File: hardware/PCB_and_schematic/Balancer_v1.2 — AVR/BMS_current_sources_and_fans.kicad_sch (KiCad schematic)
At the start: 87 parts, among them J11 HEATSING_TEMP1, J14 LOAD_RESISTOR, J15 LOAD_RESISTOR, J3 Conn_01x03, J4 HEATSING_TEMP1, J5 FAN1, J6 FAN2, J7 BATT_12V, Q10 BC807, Q11 BC817, Q12 BC817, Q13 BD238, Q14 BC807, Q15 BC817, Q16 BD238, Q18 IRF540N, Q25 IRF540N, Q9 BC817, U1 LM324, U2 74AHCT125, U3 LM358

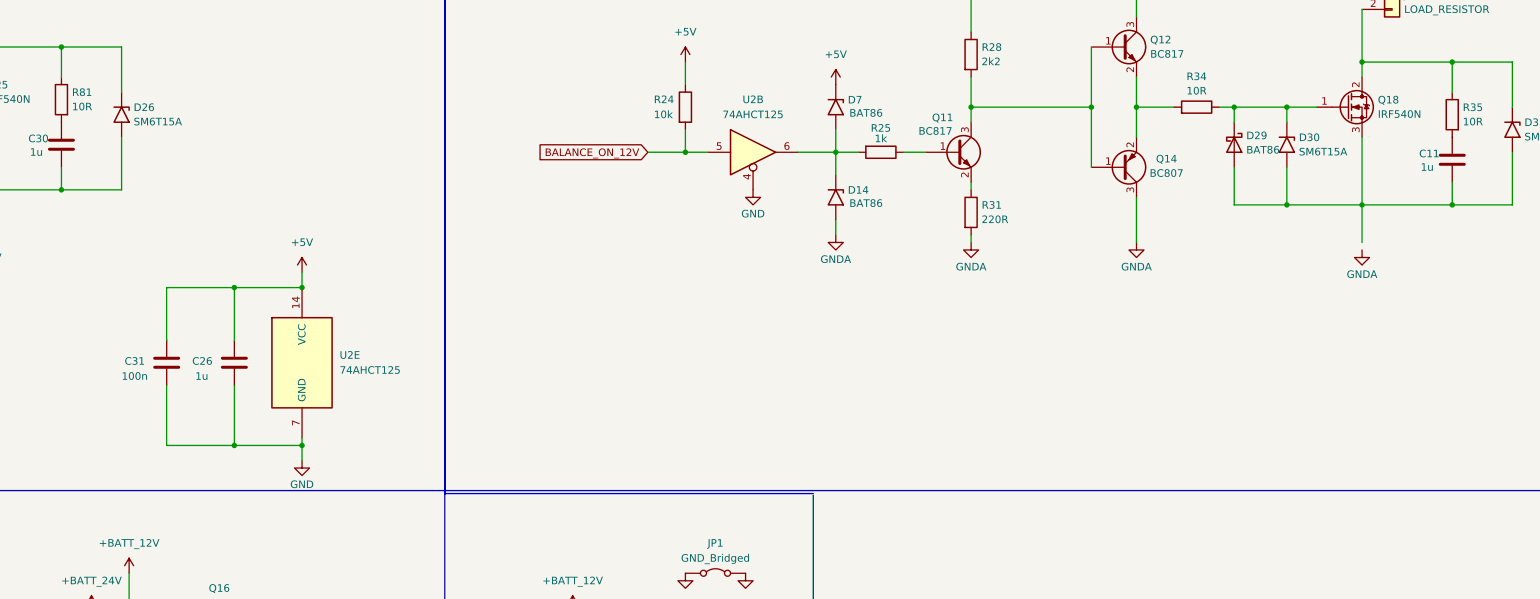
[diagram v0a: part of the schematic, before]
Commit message: Balancer PCB routing
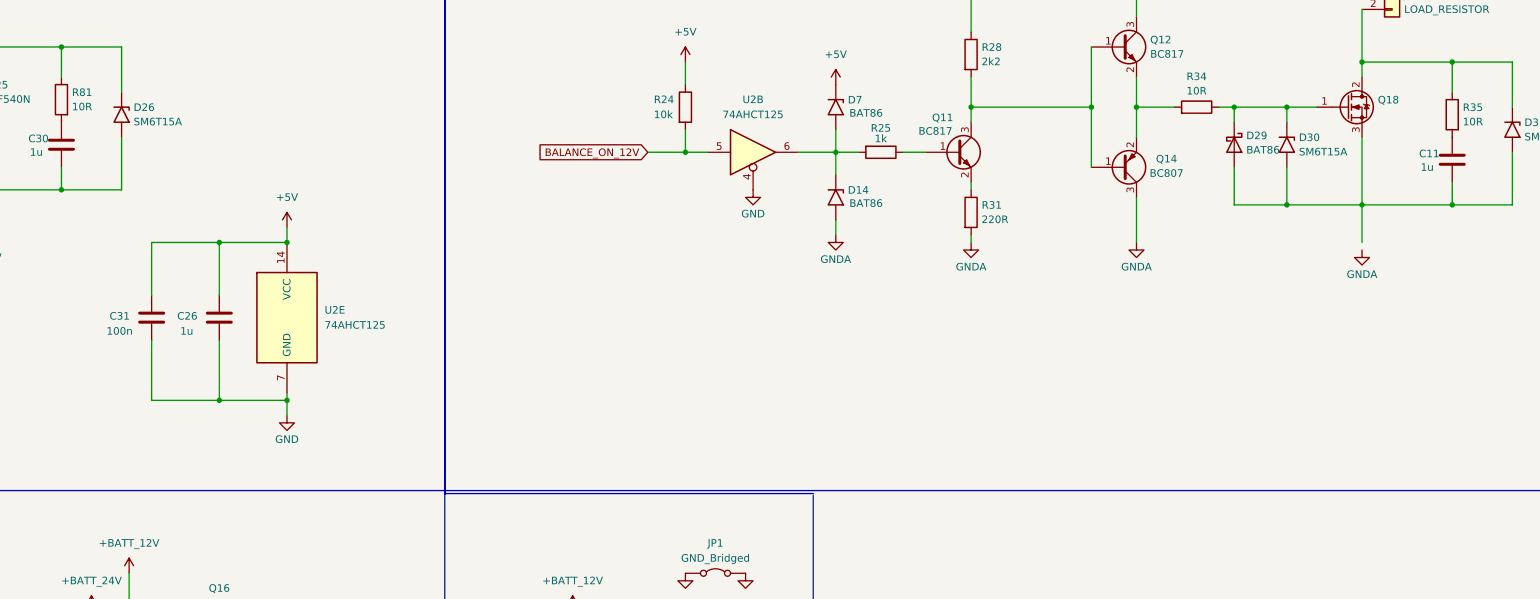
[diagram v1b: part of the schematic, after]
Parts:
- C11, C30: footprint Capacitor_SMD:C_0805_2012Metric_Pad1.18x1.45mm_HandSolder -> Capacitor_THT:C_Disc_D5.0mm_W2.5mm_P2.50mm
- D29: footprint Diode_THT:D_DO-35_SOD27_P7.62mm_Horizontal -> Diode_SMD:D_MiniMELF
- Q13, Q16: footprint My-Footprints:TO-220-3_Vertical-little-bigger pads -> Package_TO_SOT_SMD:SOT-89-3
- R35, R81: footprint Resistor_SMD:R_0805_2012Metric_Pad1.20x1.40mm_HandSolder -> Resistor_THT:R_Axial_DIN0204_L3.6mm_D1.6mm_P7.62mm_Horizontal
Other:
- moved on the sheet: C26, C31, U2E

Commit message: update balancer pcb - add gnd vdrop opamp
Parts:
- removed C7: 100n, Capacitor_SMD:C_0805_2012Metric_Pad1.18x1.45mm_HandSolder, symbol Device:C
- added C37, C39, C40: 100n, Capacitor_SMD:C_0805_2012Metric_Pad1.18x1.45mm_HandSolder, symbol Device:C
- added R60, R61, R62, R63, R66, R67: 10k/1%, Resistor_SMD:R_0805_2012Metric_Pad1.20x1.40mm_HandSolder, symbol Device:R
- added R71: 100R, Resistor_SMD:R_0805_2012Metric_Pad1.20x1.40mm_HandSolder, symbol Device:R
- added U14: LMV358, symbol Amplifier_Operational:LMV358
- U3: footprint Package_SO:SO-8_3.9x4.9mm_P1.27mm -> (none)
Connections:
- net +5V: now also C39.1, U14.8 (V+)
- net +BATT_12V: no longer C5.1, C6.1, Q12.3 (C), R28.1
- net +BATT_24V: no longer C28.1, C29.1, Q9.3 (C), R69.1, U3.8 (V+)
- net GND: now also C37.2, C39.2, C40.2, R62.2, R67.2, U14.4 (V-)
- net GNDA: now also C11.2, D29.2 (A), D30.2 (A2), D31.2 (A2), Q18.3 (S)
- net at C9.1, R30.2, R33.2: now also U3.3 (+); no longer U3.5 (+)
- net at C12.1, R50.2: now also U3.7; no longer U3.1
- net at C13.1, R38.2: now also U3.1; no longer U3.7
- net at C13.2, R40.1: now also U3.2 (-); no longer U3.6 (-)
- net at C12.2, R39.1: now also U3.6 (-); no longer U3.2 (-)
- net at C8.1, R29.2, R32.2: now also U3.5 (+); no longer U3.3 (+)
- new net: R60.2, U14.1, U14.2 (-)
- new net: C37.1, R66.2, R67.1, U14.3 (+)
- new net: R63.1, R71.2, U14.7
- new net: R60.1, R61.1, U14.5 (+)
- new net: R62.1, R63.2, U14.6 (-)
- new net +12V_LOCAL: C5.1, C6.1, Q12.3 (C), R28.1
- new net +24V_LOCAL: C28.1, C29.1, C40.1, Q9.3 (C), R69.1, U3.8 (V+)
- new net GND_VOLTAGE_DROP_ADC: R71.1
- new net GND_VOLTAGE_DROP_INPUT: R61.2
- new net VREF: R66.1
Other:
- note added: "1,25V"
- moved on the sheet: C10, C27

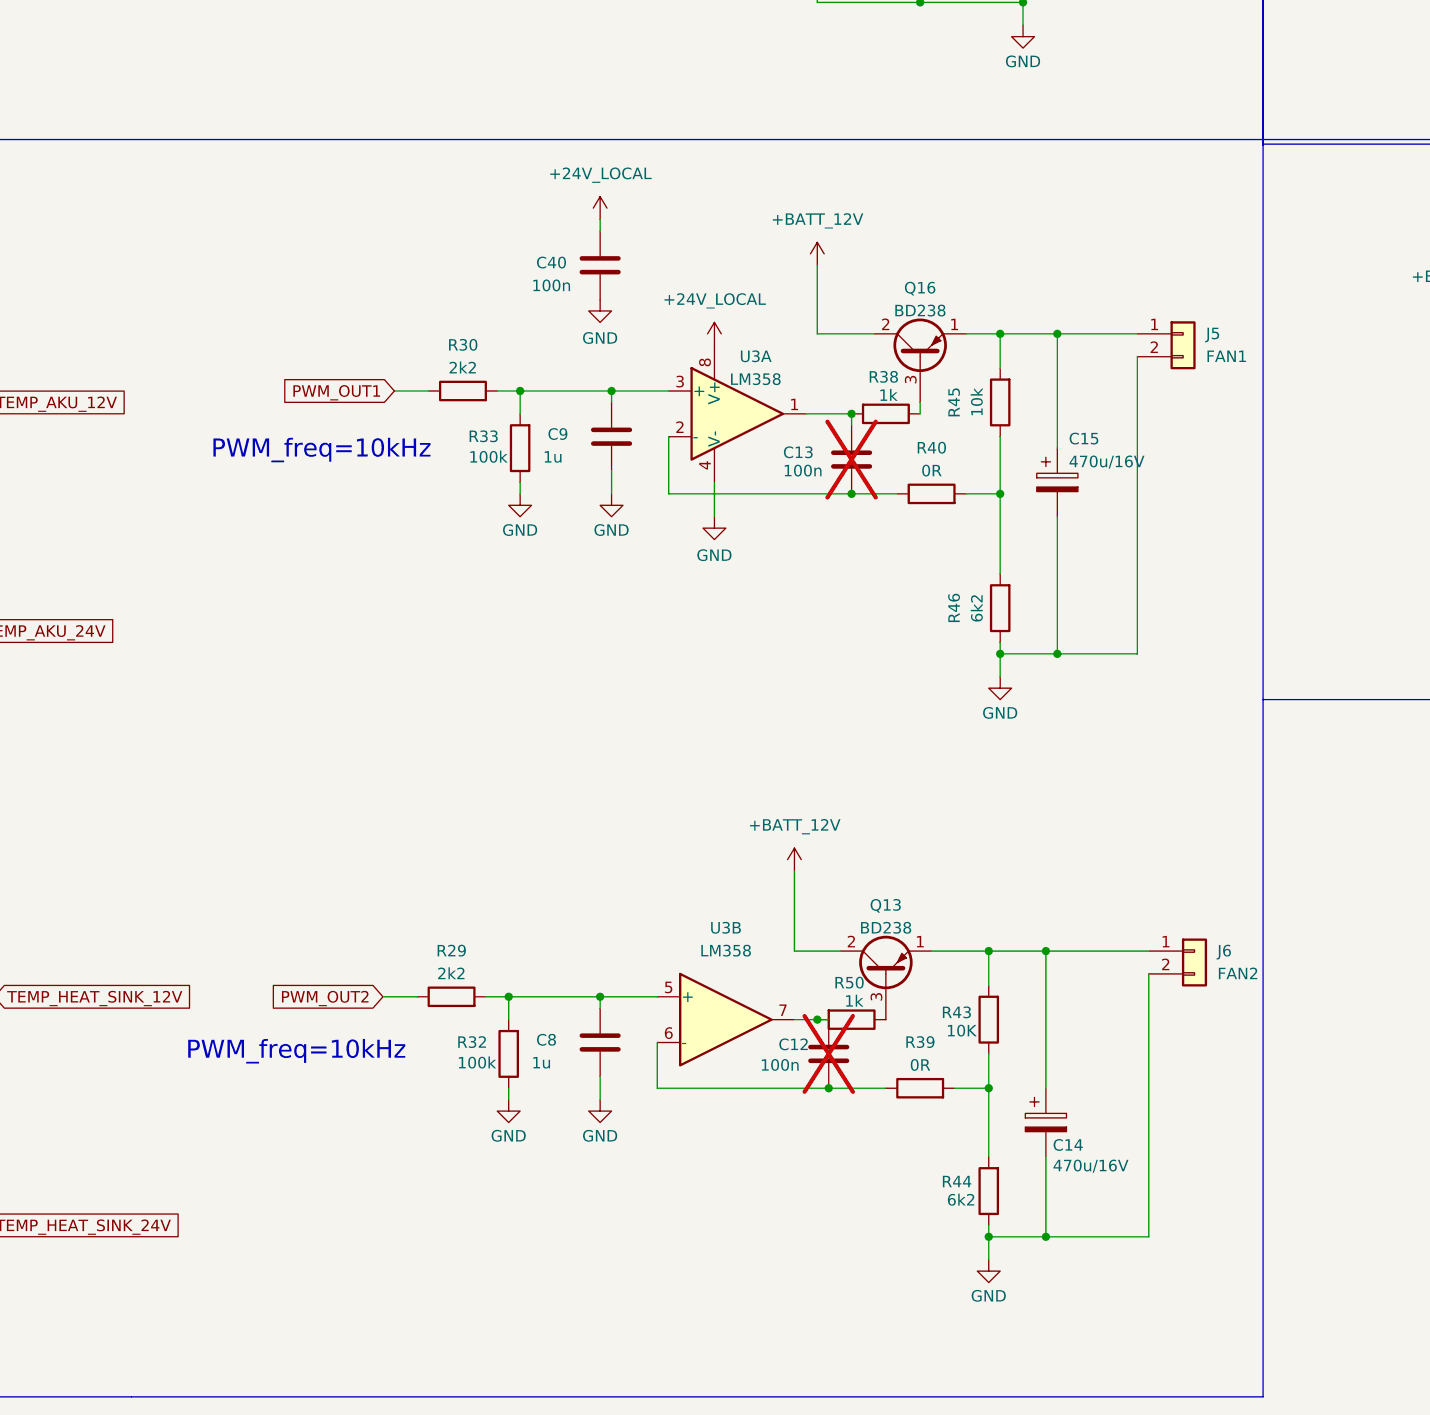
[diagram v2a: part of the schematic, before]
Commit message: Update balacer schematic - change fan drive circuit,  fix current limiter drive
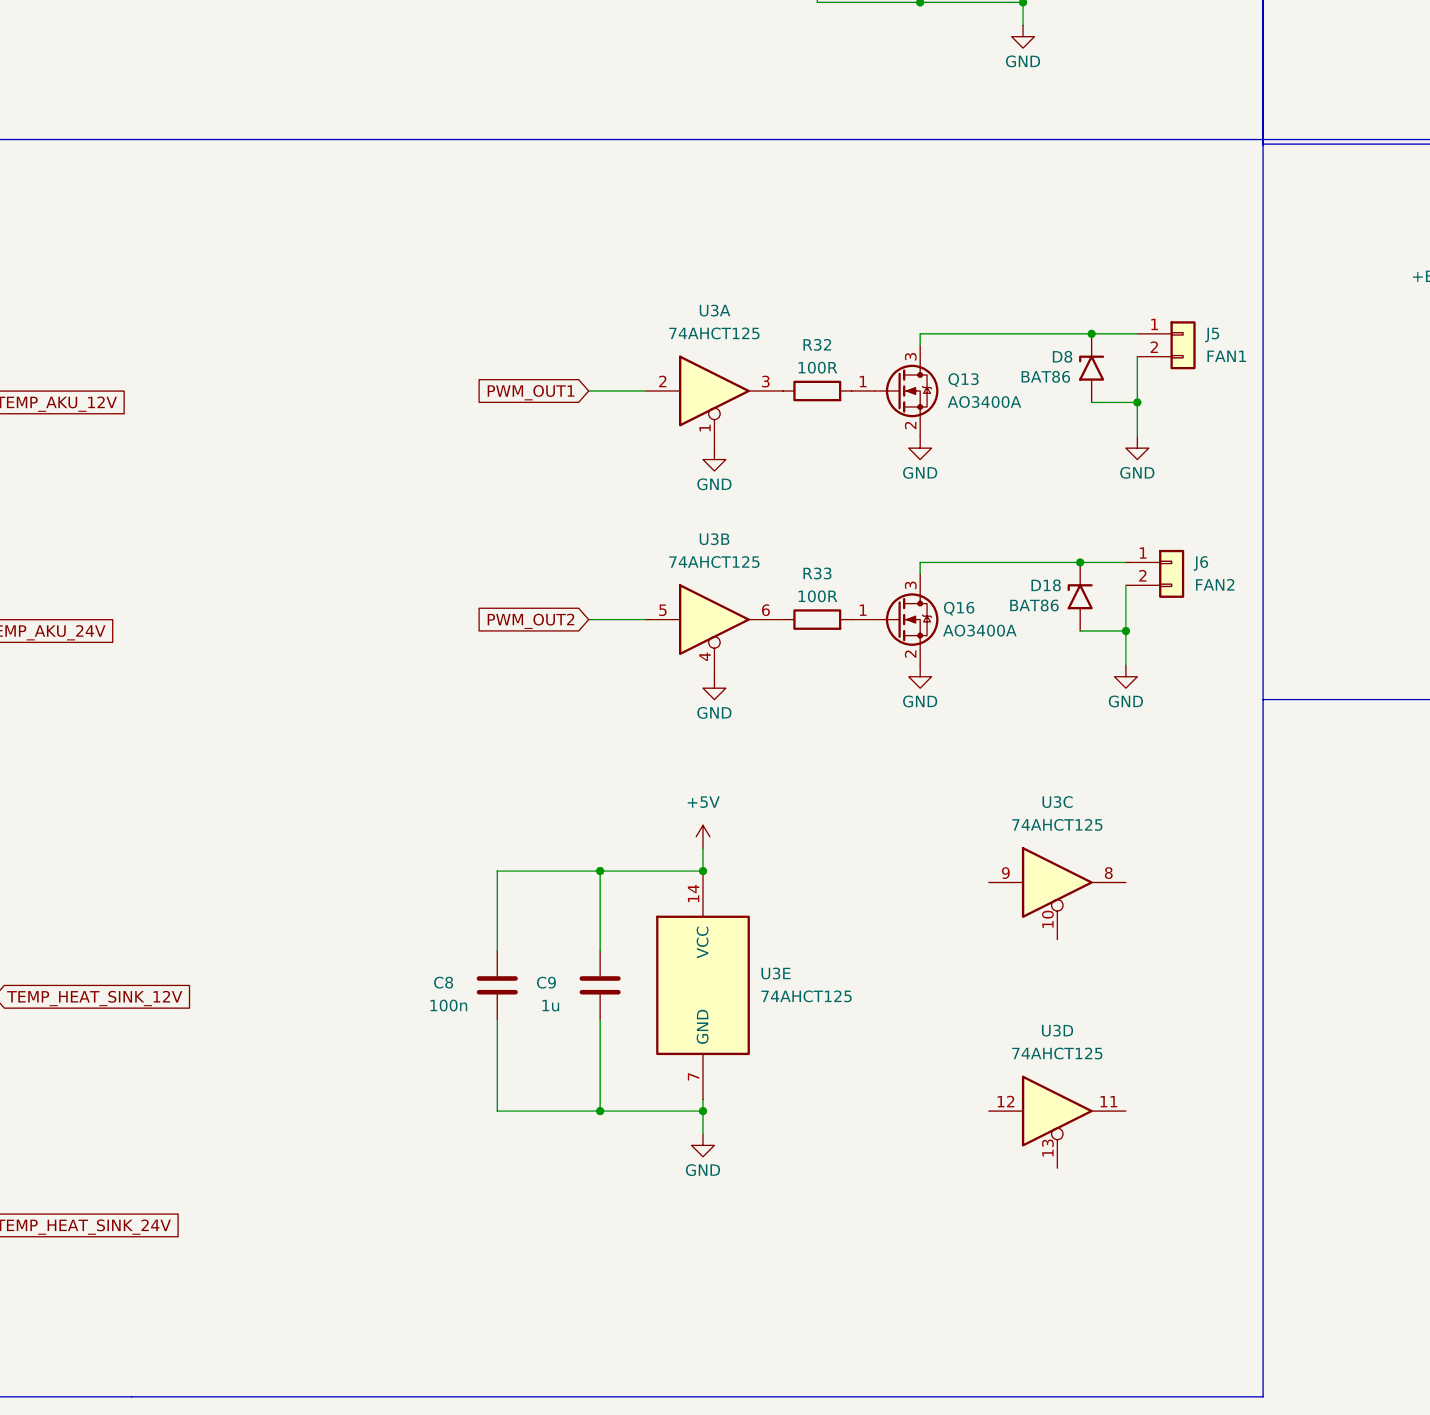
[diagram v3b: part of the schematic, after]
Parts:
- removed C12, C13, C40: 100n, Capacitor_SMD:C_0805_2012Metric_Pad1.18x1.45mm_HandSolder, symbol Device:C
- removed C14, C15: 470u/16V, Capacitor_THT:CP_Radial_D8.0mm_P2.50mm, symbol Device:C_Polarized
- removed Q13, Q16: BD238, Package_TO_SOT_SMD:SOT-89-3, symbol Transistor_BJT:BD238
- removed R29, R30: 2k2, Resistor_SMD:R_0805_2012Metric_Pad1.20x1.40mm_HandSolder, symbol Device:R
- removed R38, R50: 1k, Resistor_SMD:R_0805_2012Metric_Pad1.20x1.40mm_HandSolder, symbol Device:R
- removed R39, R40: 0R, Resistor_SMD:R_0805_2012Metric_Pad1.20x1.40mm_HandSolder, symbol Device:R
- removed R43: 10K, Resistor_SMD:R_0805_2012Metric_Pad1.20x1.40mm_HandSolder, symbol Device:R
- removed R44, R46: 6k2, Resistor_SMD:R_0805_2012Metric_Pad1.20x1.40mm_HandSolder, symbol Device:R
- removed R45: 10k, Resistor_SMD:R_0805_2012Metric_Pad1.20x1.40mm_HandSolder, symbol Device:R
- removed U3: LM358, symbol Amplifier_Operational:LM358
- added D18, D8: BAT86, Diode_SMD:D_MiniMELF, symbol Diode:SM6T15A
- added Q13, Q16: AO3400A, Package_TO_SOT_SMD:SOT-23, symbol Transistor_FET:AO3400A
- added U3: 74AHCT125, symbol 74xx:74AHCT125
- C8: value 1u -> 100n
- R32, R33: value 100k -> 100R
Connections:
- net +5V: now also C8.1, C9.1, U3.14 (VCC)
- net GND: now also D18.2 (A2), D8.2 (A2), Q13.2 (S), Q16.2 (S), U3.1, U3.4, U3.7 (GND); no longer R32.1, R33.1
- net PWM_OUT1: now also U3.2
- net PWM_OUT2: now also U3.5
- net at J6.1 (Pin_1): now also D18.1 (A1), Q16.3 (D)
- net at R33.2: now also Q16.1 (G); no longer C9.1
- net at R32.2: now also Q13.1 (G); no longer C8.1
- net at J5.1 (Pin_1): now also D8.1 (A1), Q13.3 (D)
- new net: R33.1, U3.6
- new net: R32.1, U3.3
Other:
- note removed: "PWM_freq=10kHz"
- moved on the sheet: J6
